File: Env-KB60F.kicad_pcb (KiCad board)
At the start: 2 copper layers, 125 parts, among them U1 Pico

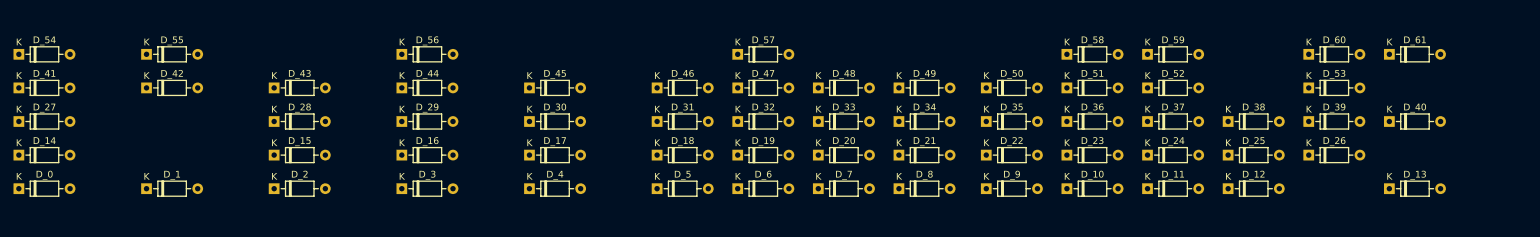
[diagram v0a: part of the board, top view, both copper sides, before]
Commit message: Aligned diodes as preferred
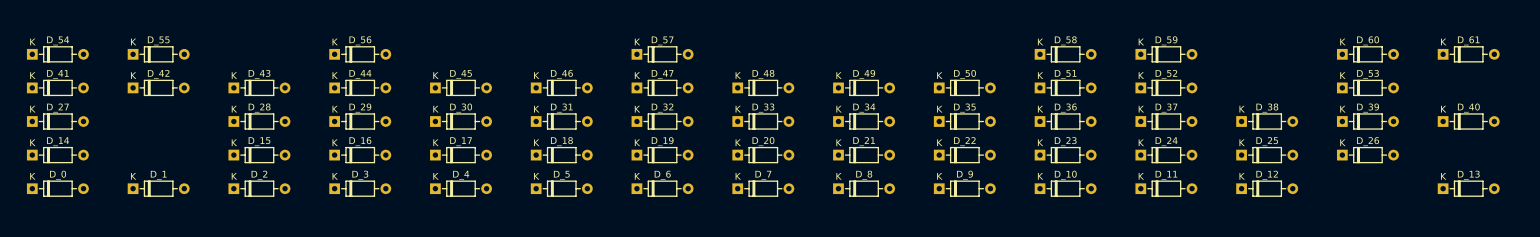
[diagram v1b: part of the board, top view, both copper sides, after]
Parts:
- moved D_18 18.0 mm to (157.4, 55.0)
- moved D_31 18.0 mm to (157.4, 50.0)
- moved D_46 18.0 mm to (157.4, 45.0)
- moved D_5 18.0 mm to (157.4, 60.0)
- moved D_19 15.0 mm to (172.4, 55.0)
- moved D_32 15.0 mm to (172.4, 50.0)
- moved D_47 15.0 mm to (172.4, 45.0)
- moved D_57 15.0 mm to (172.4, 40.0)
- moved D_6 15.0 mm to (172.4, 60.0)
- moved D_17 14.0 mm to (142.4, 55.0)
- moved D_30 14.0 mm to (142.4, 50.0)
- moved D_4 14.0 mm to (142.4, 60.0)
- moved D_45 14.0 mm to (142.4, 45.0)
- moved D_20 12.0 mm to (187.4, 55.0)
- moved D_33 12.0 mm to (187.4, 50.0)
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
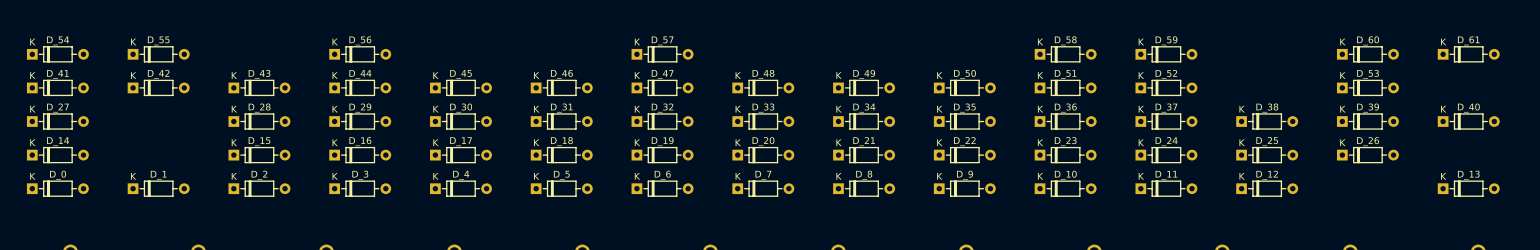
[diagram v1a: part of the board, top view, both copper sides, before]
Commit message: Diodes were wrong direction
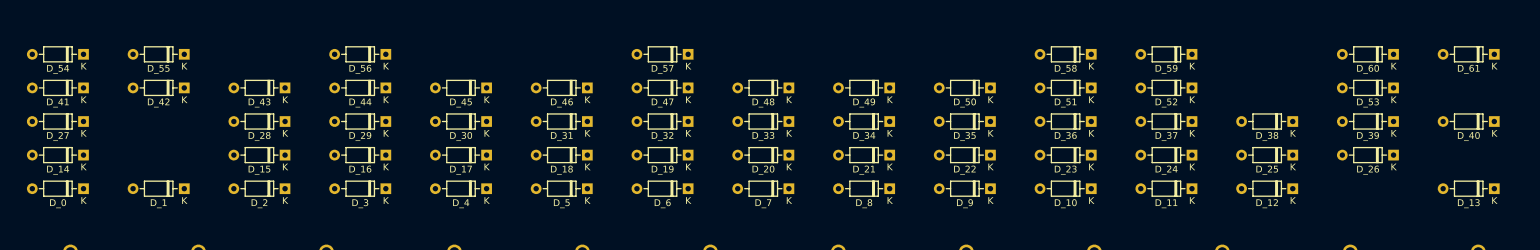
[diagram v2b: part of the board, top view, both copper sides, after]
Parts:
- moved D_0 7.62 mm to (90.0, 60.0), turned to 180 degrees
- moved D_1 7.62 mm to (105.0, 60.0), turned to 180 degrees
- moved D_10 7.62 mm to (240.0, 60.0), turned to 180 degrees
- moved D_11 7.62 mm to (255.0, 60.0), turned to 180 degrees
- moved D_12 7.62 mm to (270.0, 60.0), turned to 180 degrees
- moved D_13 7.62 mm to (300.0, 60.0), turned to 180 degrees
- moved D_14 7.62 mm to (90.0, 55.0), turned to 180 degrees
- moved D_15 7.62 mm to (120.0, 55.0), turned to 180 degrees
- moved D_16 7.62 mm to (135.0, 55.0), turned to 180 degrees
- moved D_17 7.62 mm to (150.0, 55.0), turned to 180 degrees
- moved D_18 7.62 mm to (165.0, 55.0), turned to 180 degrees
- moved D_19 7.62 mm to (180.0, 55.0), turned to 180 degrees
- moved D_2 7.62 mm to (120.0, 60.0), turned to 180 degrees
- moved D_20 7.62 mm to (195.0, 55.0), turned to 180 degrees
- moved D_21 7.62 mm to (210.0, 55.0), turned to 180 degrees
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
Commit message: Added More traces n stuff
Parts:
- moved D_0 20.1 mm to (110.0, 58.0)
- moved D_14 20.1 mm to (110.0, 53.0)
- moved D_27 20.1 mm to (110.0, 48.0)
- moved D_41 20.1 mm to (110.0, 43.0)
- moved D_54 20.1 mm to (110.0, 38.0)
- moved D_1 19.1 mm to (124.0, 58.0)
- moved D_42 19.1 mm to (124.0, 43.0)
- moved D_55 19.1 mm to (124.0, 38.0)
- moved D_15 18.1 mm to (138.0, 53.0)
- moved D_2 18.1 mm to (138.0, 58.0)
- moved D_28 18.1 mm to (138.0, 48.0)
- moved D_43 18.1 mm to (138.0, 43.0)
- moved D_16 17.1 mm to (152.0, 53.0)
- moved D_29 17.1 mm to (152.0, 48.0)
- moved D_3 17.1 mm to (152.0, 58.0)
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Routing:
- net Net-(D_60-Pad2): track 0.00 -> 150.2 mm
- net Net-(D_61-Pad2): track 0.00 -> 145.0 mm
- net Net-(D_59-Pad2): track 0.00 -> 142.0 mm
- net Net-(D_58-Pad2): track 0.00 -> 136.4 mm
- net Net-(D_53-Pad2): track 0.00 -> 127.3 mm
- net Net-(D_57-Pad2): track 0.00 -> 122.2 mm
- net Net-(D_52-Pad2): track 0.00 -> 117.7 mm
- net Net-(D_56-Pad2): track 0.00 -> 117.0 mm
- net Net-(D_43-Pad2): track 0.00 -> 113.1 mm
- net Net-(D_51-Pad2): track 0.00 -> 110.8 mm
- net Net-(D_49-Pad2): track 0.00 -> 107.7 mm
- net Net-(D_50-Pad2): track 0.00 -> 104.7 mm
- net Net-(D_48-Pad2): track 0.00 -> 101.3 mm
- net Net-(D_39-Pad2): track 0.00 -> 99.9 mm
- net Net-(D_47-Pad2): track 0.00 -> 96.8 mm
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
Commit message: General Re-doing of stuff
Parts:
- added G***: LOGO, AKLogo:logo, F.Cu at (327.5, 49.5)
- moved D_0 7.16 mm to (103.0, 56.5)
- moved D_1 7.16 mm to (117.0, 56.5)
- moved D_10 7.16 mm to (243.0, 56.5)
- moved D_11 7.16 mm to (257.0, 56.5)
- moved D_12 7.16 mm to (271.0, 56.5)
- moved D_13 7.16 mm to (299.0, 56.5)
- moved D_14 7.16 mm to (103.0, 51.5)
- moved D_15 7.16 mm to (131.0, 51.5)
- moved D_16 7.16 mm to (145.0, 51.5)
- moved D_17 7.16 mm to (159.0, 51.5)
- moved D_18 7.16 mm to (173.0, 51.5)
- moved D_19 7.16 mm to (187.0, 51.5)
- moved D_2 7.16 mm to (131.0, 56.5)
- moved D_20 7.16 mm to (201.0, 51.5)
- moved D_21 7.16 mm to (215.0, 51.5)
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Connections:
- U1 pad 10: Net-(U1-Pad10) -> col3
- U1 pad 11: Net-(U1-Pad11) -> col2
- U1 pad 12: Net-(U1-Pad12) -> col1
- U1 pad 13: Net-(U1-Pad13) -> GND
- U1 pad 14: Net-(U1-Pad14) -> col0
- U1 pad 15: Net-(U1-Pad15) -> row0
- U1 pad 16: Net-(U1-Pad16) -> row1
- U1 pad 17: Net-(U1-Pad17) -> row2
- U1 pad 18: Net-(U1-Pad18) -> GND
- U1 pad 19: Net-(U1-Pad19) -> row3
- U1 pad 20: Net-(U1-Pad20) -> row4
- U1 pad 21: Net-(U1-Pad21) -> col6
- U1 pad 22: Net-(U1-Pad22) -> col7
- U1 pad 23: Net-(U1-Pad23) -> GND
- U1 pad 24: Net-(U1-Pad24) -> col8
- U1 pad 25: Net-(U1-Pad25) -> col9
- U1 pad 26: Net-(U1-Pad26) -> col10
- U1 pad 27: Net-(U1-Pad27) -> col11
- U1 pad 28: Net-(U1-Pad28) -> GND
- U1 pad 29: Net-(U1-Pad29) -> col12
- U1 pad 3: Net-(U1-Pad3) -> GND
- U1 pad 31: Net-(U1-Pad31) -> col13
- U1 pad 32: Net-(U1-Pad32) -> col14
- U1 pad 38: Net-(U1-Pad38) -> GND
- U1 pad 7: Net-(U1-Pad7) -> col5
- U1 pad 8: Net-(U1-Pad8) -> GND
- U1 pad 9: Net-(U1-Pad9) -> col4
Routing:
- net col0: track 82.2 -> 346.2 mm
- net col1: track 79.2 -> 328.2 mm
- net row0: track 0.00 -> 246.2 mm
- net row1: track 0.00 -> 235.7 mm
- net row2: track 0.00 -> 231.6 mm
- net col2: track 67.6 -> 298.7 mm
- net row3: track 0.00 -> 222.9 mm
- net row4: track 0.00 -> 220.7 mm
- net col3: track 92.0 -> 305.6 mm
- net col4: track 67.5 -> 264.2 mm
- net col5: track 67.7 -> 251.1 mm
- net col6: track 87.7 -> 207.4 mm
- net col7: track 67.6 -> 170.8 mm
- net col8: track 67.5 -> 158.0 mm
- net col9: track 67.5 -> 141.4 mm
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- added copper zone on B.Cu, net GND
- added copper zone on F.Cu, net GND
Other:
- board outline added: 283 x 126.1 mm

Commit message: Added some mount holes n stuff
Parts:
- added H1: MountingHole, MountingHole:MountingHole_2.2mm_M2, F.Cu at (220.0, 150.0)
- added H2: MountingHole, MountingHole:MountingHole_2.2mm_M2, F.Cu at (86.0, 40.0)
- added H3: MountingHole, MountingHole:MountingHole_2.2mm_M2, F.Cu at (338.0, 141.5)
- added H4: MountingHole, MountingHole:MountingHole_2.2mm_M2, F.Cu at (80.6, 141.2)
- added H5: MountingHole, MountingHole:MountingHole_2.2mm_M2, F.Cu at (238.0, 84.0)
- added H6: MountingHole, MountingHole:MountingHole_2.2mm_M2, F.Cu at (336.0, 87.0)
- added H7: MountingHole, MountingHole:MountingHole_2.2mm_M2, F.Cu at (305.0, 37.0)
- moved G*** 240.5 mm to (87.0, 53.0)
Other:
- board text added: "-> USB"
- board text added: "Env-KB60F"
- board text added: "https://github.com/Envious-Data/Env-KB60F"

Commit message: Spotted a lil derp and fixed it
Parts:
- moved H3 3.00 mm to (338.0, 144.5)

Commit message: Added some stuff
Added a Button for reset and also a bunch of silkscreen instructions for building the keyboard aswell as a QR Code URL that brings you to this Repository.
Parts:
- added G***: LOGO, AKLogo:githubqrcode, B.Cu at (346.0, 49.0)
- added G***: LOGO, AKLogo:diode, F.Cu at (317.5, 49.5)
- added SW1: EVQ-P7A01P, PanasonicEVQ-P7A01P:Panasonic-EVQ-P7A01P-0-0-MFG, F.Cu at (358.7, 74.5)
- moved G*** 5.80 mm to (87.8, 58.8)
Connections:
- U1 pad 30: Net-(U1-Pad30) -> RUNPIN
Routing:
- net RUNPIN: track 0.00 -> 39.0 mm
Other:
- board text added: ">"
- board text added: "All diodes on this board have the same orientation"
- board text added: "Diodes will usually have a stripe on one side. that side is the cathode side."
- board text added: "Envious.Media"
- board text added: "If you are using "5 Pin" switches please ensure they are popped into the PCB properly before soldering"
- board text added: "RESET MCU"
- board text added: "Scan for GitHub URL http://github.com/envious-data/env-kb60f"
- board text added: "The Raspberry Pi Pico should be soldered with the usb to the right"
- board text added: "USB >"
- board text removed: "-> USB"
- board text removed: "https://github.com/Envious-Data/Env-KB60F"

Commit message: Changed QR Code
meh its a easter egg now.
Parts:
- removed the G*** at (346.0, 49.0)
- added G***: LOGO, AKLogo:UnwantedQR, B.Cu at (345.0, 49.0)
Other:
- board text added: "http://github.com/envious-data/env-kb60f"
- board text removed: "Scan for GitHub URL http://github.com/envious-data/env-kb60f"
